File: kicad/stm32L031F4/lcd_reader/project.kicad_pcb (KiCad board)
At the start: 2 copper layers, 33 x 25.4 mm, 32 parts, among them J1 WAKE, J10 TEST_1P, J11 TEST_1P, J12 TEST_1P, J2 SWD, J3 TEST_1P, J4 TEST_1P, J5 TEST_1P, J6 LCD, J7 TEST_1P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

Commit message: All connected
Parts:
- moved R2 15.2 mm to (191.8, 137.1)
- moved R1 2.02 mm to (190.9, 121.8)
- renumbered J1 to WAKE
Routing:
- net +BATT: track 20.2 -> 98.6 mm, vias 0 -> 1
- net GND: track 65.7 -> 127.4 mm, vias 0 -> 8
- net Net-(Q1-Pad4): track 19.7 -> 1.93 mm, vias 2 -> 0
- net RADIO_PWR: track 3.43 -> 14.6 mm, vias 0 -> 2
- net Net-(J6-Pad7): track 10.8 -> 13.5 mm
- net Net-(J6-Pad5): track 10.5 -> 8.14 mm, vias 0 -> 1
- net Net-(J6-Pad6): track 12.4 -> 10.1 mm
- net Net-(J6-Pad4): track 12.8 -> 10.7 mm, vias 0 -> 1
- net Net-(J6-Pad1): track 11.0 -> 9.19 mm, vias 0 -> 1
- net IN8: track 29.3 -> 30.6 mm
- net TX: track 13.6 -> 14.7 mm
- net Net-(J6-Pad3): track 14.1 -> 15.0 mm
- net SWDIO: track 10.8 -> 11.7 mm
- net Net-(J6-Pad2): track 12.6 -> 13.4 mm
- net Net-(R1-Pad1): track 4.16 -> 3.42 mm
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- added copper zone on B.Cu, net GND
- added copper zone on F.Cu, net GND
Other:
- net class Default: clearance 0.2032 -> 0.2
- rule trace_clearance: 0.2032 -> 0.2

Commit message: Labels
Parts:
- added J13: GND_EXT, Pin_Headers:Pin_Header_Straight_1x01_Pitch2.54mm, F.Cu at (199.4, 141.0)
- renumbered WAKE to J1
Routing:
- net GND: track 127.4 -> 130.4 mm
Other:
- board text added: "+"
- board text added: "-"
- board text added: "CLK"
- board text added: "COM1"
- board text added: "DIO"
- board text added: "FET"
- board text added: "GND"
- board text added: "RDY"
- board text added: "RST"
- board text added: "SWD"
- board text added: "TX"
- board text added: "VCC"
- board text added: "WAKE"

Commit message: Logos
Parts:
- added REF**: TheApiLogo, theapi:TheApiLogoSmall, B.Cu at (186.8, 121.4)
- added REF**: TheApiLogoTiny, theapi:TheApiLogoTiny, F.Cu at (199.0, 117.2)
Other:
- board text added: "github.com/theapi/bathroom_scales November 2017 v1.0"
- board text added: "github.com/theapi/bathroom_scales v1.0"

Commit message: Silkscreen tidying
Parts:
- J13: footprint Pin_Headers:Pin_Header_Straight_1x01_Pitch2.54mm -> theapi:Pin_Header_Straight_1x01_Pitch2.54mm
- J8: footprint Pin_Headers:Pin_Header_Straight_1x03_Pitch2.54mm -> theapi:Pin_Header_Straight_1x03_Pitch2.54mm
- moved J6 20.3 mm to (168.9, 141.0), turned to 180 degrees
- moved C3 0.47 mm to (188.6, 136.2)
- moved REF** 0.28 mm to (198.8, 117.4)
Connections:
- J6 pad 1: Net-(J6-Pad1) -> COM1
- J6 pad 9: COM1 -> Net-(J6-Pad9)
- R10 pad 2: Net-(J6-Pad1) -> Net-(J6-Pad9)
- R3 pad 2: Net-(J6-Pad8) -> Net-(J6-Pad2)
- R4 pad 2: Net-(J6-Pad7) -> Net-(J6-Pad3)
- R5 pad 2: Net-(J6-Pad6) -> Net-(J6-Pad4)
- R7 pad 2: Net-(J6-Pad4) -> Net-(J6-Pad6)
- R8 pad 2: Net-(J6-Pad3) -> Net-(J6-Pad7)
- R9 pad 2: Net-(J6-Pad2) -> Net-(J6-Pad8)
- U1 pad 11: Net-(J6-Pad6) -> Net-(J6-Pad4)
- U1 pad 5: Net-(J6-Pad8) -> Net-(J6-Pad2)
- U1 pad 9: Net-(J6-Pad7) -> Net-(J6-Pad3)
- U3 pad 11: Net-(J6-Pad2) -> Net-(J6-Pad8)
- U3 pad 13: Net-(J6-Pad1) -> Net-(J6-Pad9)
- U3 pad 5: Net-(J6-Pad4) -> Net-(J6-Pad6)
- U3 pad 9: Net-(J6-Pad3) -> Net-(J6-Pad7)
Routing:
- net Net-(J6-Pad9): track 0.00 -> 9.19 mm, vias 0 -> 1
- net Net-(J6-Pad1): track 9.19 -> 0.00 mm, vias 1 -> 0
- net Net-(J6-Pad7): track 13.5 -> 15.0 mm
- net Net-(J6-Pad3): track 15.0 -> 13.5 mm
- net RADIO_PWR: track 14.6 -> 15.6 mm
- net Net-(J6-Pad8): track 12.7 -> 13.4 mm, vias 0 -> 1
- net Net-(J6-Pad2): track 13.4 -> 12.7 mm, vias 1 -> 0
- net Net-(J6-Pad6): track 10.1 -> 10.7 mm
- net Net-(J6-Pad4): track 10.7 -> 10.1 mm
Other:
- board text added: "LCD"
- board text added: "o"

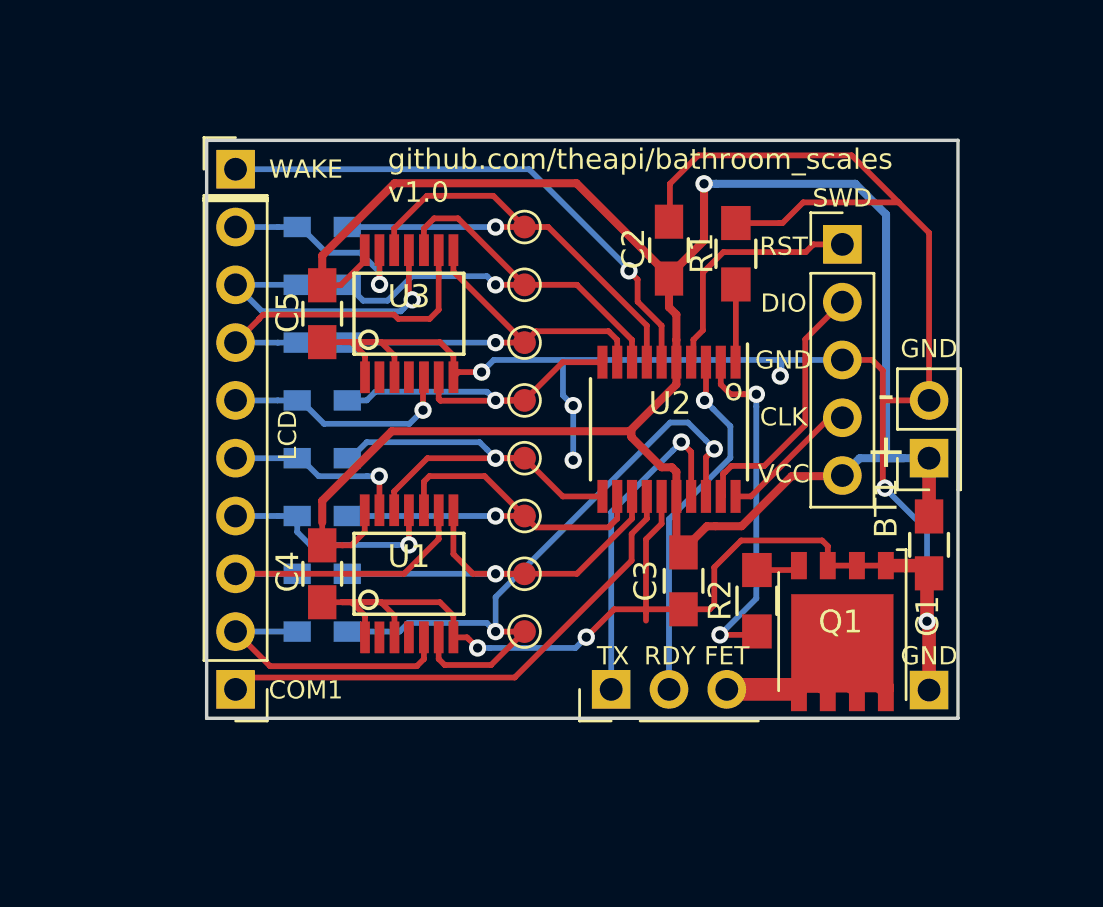
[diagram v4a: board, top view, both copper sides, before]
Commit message: Start of zebra strip compatability
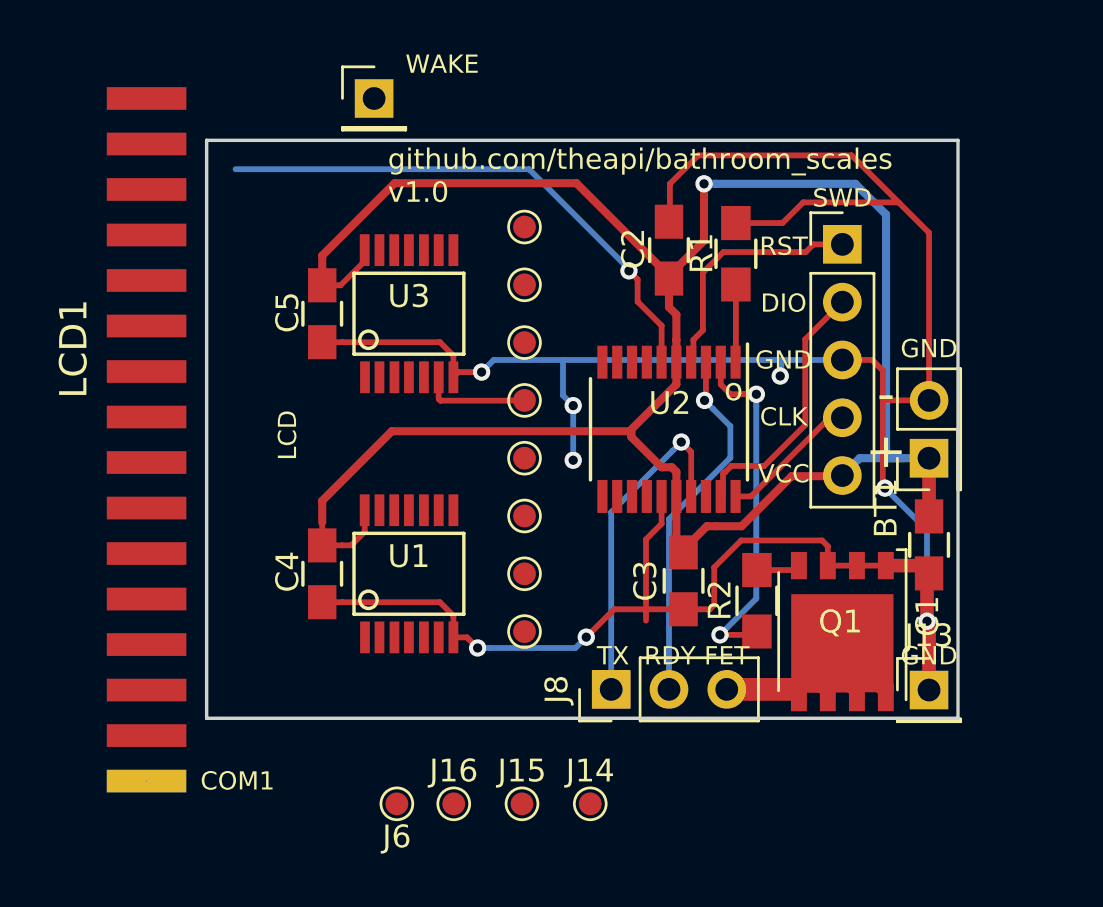
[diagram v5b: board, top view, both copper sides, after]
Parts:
- removed R10, R3, R4, R5, R6, R7, R8, R9: 0R, Resistors_SMD:R_0603_HandSoldering
- removed REF**: TheApiLogo, theapi:TheApiLogoSmall
- removed REF**: TheApiLogoTiny, theapi:TheApiLogoTiny
- added J14: TEST_1P, Connectors_TestPoints:Test_Point_Pad_d1.0mm, F.Cu at (184.5, 146.0)
- added J15: TEST_1P, Connectors_TestPoints:Test_Point_Pad_d1.0mm, F.Cu at (181.5, 146.0)
- added J16: TEST_1P, Connectors_TestPoints:Test_Point_Pad_d1.0mm, F.Cu at (178.5, 146.0)
- added LCD1: CONN_01X16, theapi:ZEBRA-16, F.Cu at (165.0, 126.0)
- J13: footprint theapi:Pin_Header_Straight_1x01_Pitch2.54mm -> Pin_Headers:Pin_Header_Straight_1x01_Pitch2.54mm
- J6: value LCD -> TEST_1P; footprint Pin_Headers:Pin_Header_Straight_1x09_Pitch2.54mm -> Connectors_TestPoints:Test_Point_Pad_d1.0mm
- J8: footprint theapi:Pin_Header_Straight_1x03_Pitch2.54mm -> Pin_Headers:Pin_Header_Straight_1x03_Pitch2.54mm
- moved J6 8.69 mm to (176.0, 146.0)
- moved J1 6.84 mm to (175.0, 115.0)
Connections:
- J6 pad 1: COM1 -> Net-(J6-Pad1)
- U1 pad 1: GND -> Net-(LCD1-Pad1)
- U1 pad 10: IN6 -> IN8
- U1 pad 11: Net-(J6-Pad4) -> Net-(LCD1-Pad5)
- U1 pad 12: IN5 -> IN7
- U1 pad 13: Net-(J6-Pad5) -> Net-(LCD1-Pad6)
- U1 pad 3: GND -> Net-(LCD1-Pad2)
- U1 pad 5: Net-(J6-Pad2) -> Net-(LCD1-Pad3)
- U1 pad 6: IN8 -> Net-(J14-Pad1)
- U1 pad 8: IN7 -> Net-(J6-Pad1)
- U1 pad 9: Net-(J6-Pad3) -> Net-(LCD1-Pad4)
- U3 pad 1: GND -> Net-(LCD1-Pad7)
- U3 pad 11: Net-(J6-Pad8) -> Net-(LCD1-Pad11)
- U3 pad 13: Net-(J6-Pad9) -> Net-(LCD1-Pad12)
- U3 pad 2: Net-(U3-Pad2) -> IN6
- U3 pad 3: GND -> Net-(LCD1-Pad8)
- U3 pad 4: Net-(U3-Pad4) -> IN5
- U3 pad 5: Net-(J6-Pad6) -> Net-(LCD1-Pad9)
- U3 pad 9: Net-(J6-Pad7) -> Net-(LCD1-Pad10)
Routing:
- net IN8: track 30.6 -> 0.00 mm, vias 2 -> 0
- net IN1: track 24.4 -> 0.00 mm, vias 1 -> 0
- net COM1: track 22.8 -> 0.00 mm
- net IN2: track 22.2 -> 0.00 mm, vias 1 -> 0
- net IN7: track 19.9 -> 0.00 mm, vias 1 -> 0
- net IN6: track 19.7 -> 0.00 mm, vias 1 -> 0
- net IN5: track 19.7 -> 0.00 mm, vias 1 -> 0
- net IN3: track 18.6 -> 0.00 mm, vias 1 -> 0
- net Net-(J6-Pad7): track 15.0 -> 0.00 mm
- net Net-(J6-Pad3): track 13.5 -> 0.00 mm
- net Net-(J6-Pad8): track 13.4 -> 0.00 mm, vias 1 -> 0
- net Net-(J6-Pad2): track 12.7 -> 0.00 mm
- net IN4: track 17.0 -> 4.76 mm, vias 1 -> 0
- net GND: track 130.0 -> 118.7 mm
- net Net-(J6-Pad6): track 10.7 -> 0.00 mm, vias 1 -> 0
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
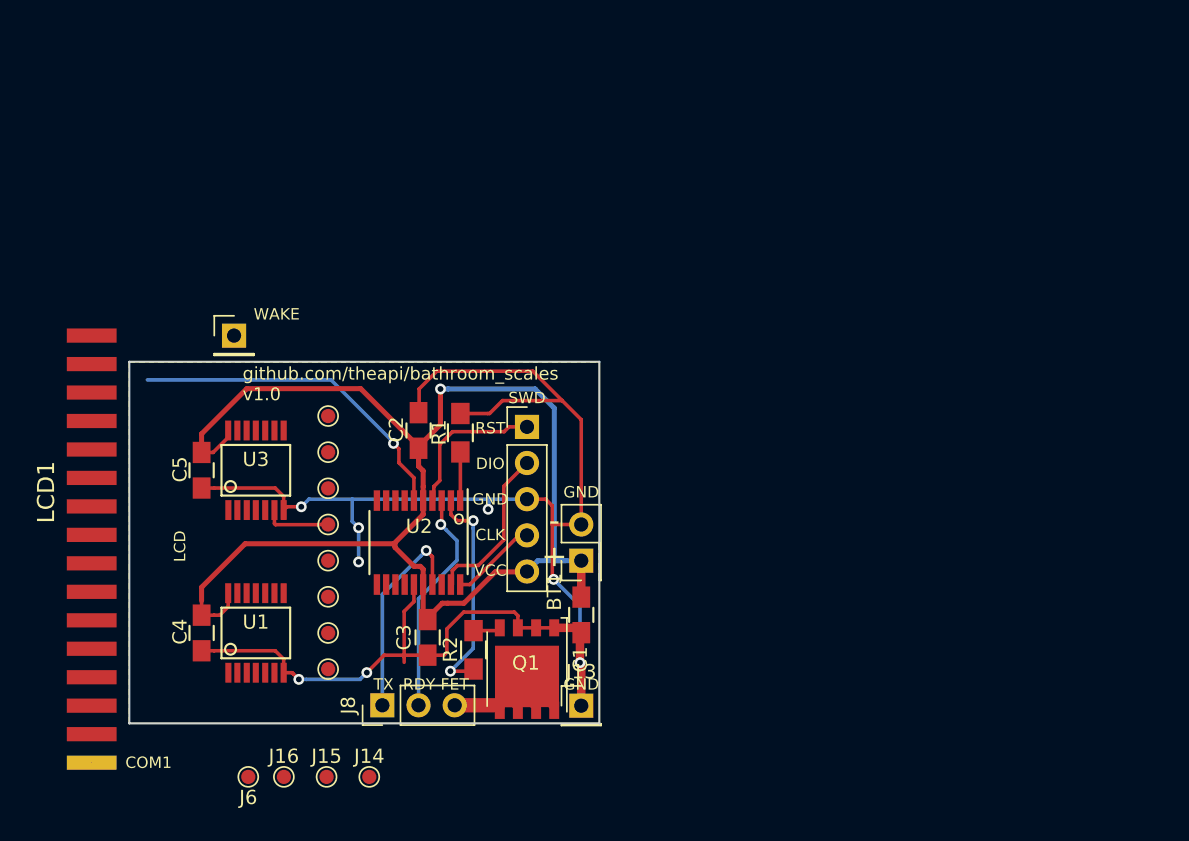
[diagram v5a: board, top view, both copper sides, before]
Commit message: Layout for sandwiched zebra connector
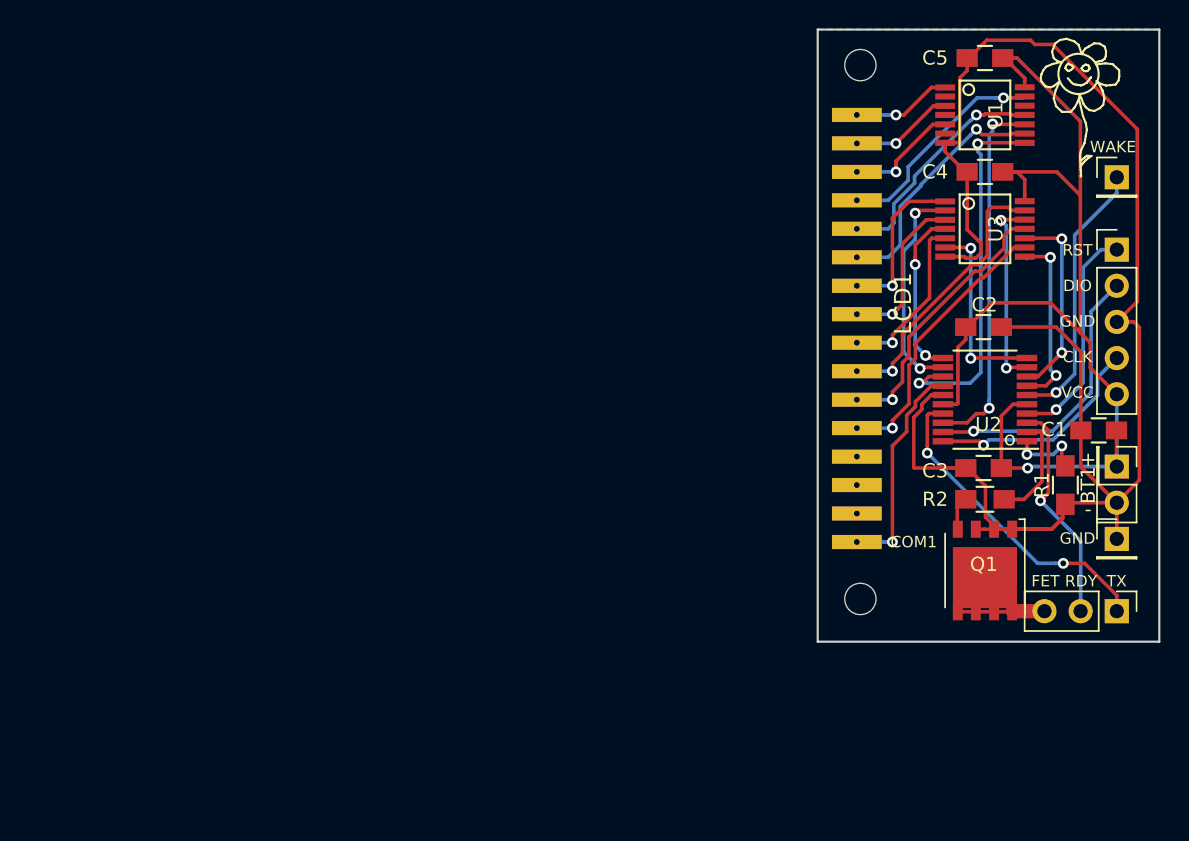
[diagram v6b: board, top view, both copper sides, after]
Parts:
- removed J10, J11, J12, J14, J15, J16, J3, J4, J5, J6, J7, J9: TEST_1P, Connectors_TestPoints:Test_Point_Pad_d1.0mm
- added REF**: MountingHole_2.2mm_M2, Mounting_Holes:MountingHole_2.2mm_M2, F.Cu at (219.0, 133.5)
- added REF**: TheApiLogo, theapi:TheApiLogoSmall, F.Cu at (235.0, 93.8)
- added REF**: TheApiLogoTiny, theapi:TheApiLogoTiny, F.Cu at (223.5, 130.8)
- added REF**: TheApiLogo, theapi:TheApiLogoSmall, B.Cu at (233.8, 129.5)
- added REF**: MountingHole_2.2mm_M2, Mounting_Holes:MountingHole_2.2mm_M2, F.Cu at (219.0, 96.0)
- moved C4 63.9 mm to (227.8, 103.5), turned to 0 degrees
- moved J1 63.0 mm to (237.0, 103.9)
- moved U1 62.8 mm to (227.8, 99.5), turned to 270 degrees
- moved C5 62.2 mm to (227.8, 95.5), turned to 0 degrees
- moved LCD1 55.9 mm to (218.8, 110.5)
- moved U3 54.0 mm to (227.8, 107.5), turned to 270 degrees
- moved J8 52.0 mm to (237.0, 134.4), turned to 270 degrees
- moved J2 43.3 mm to (237.0, 109.0)
- moved R1 42.7 mm to (233.4, 125.5), turned to 270 degrees
- moved U2 41.0 mm to (227.8, 119.5), turned to 180 degrees
- moved C3 40.8 mm to (227.7, 124.3), turned to 0 degrees
- moved C2 40.3 mm to (227.7, 114.4), turned to 0 degrees
- moved J13 39.4 mm to (237.0, 129.3)
- moved C1 38.6 mm to (235.7, 121.7), turned to 180 degrees
- moved BT1 38.2 mm to (237.0, 124.2), turned to 270 degrees
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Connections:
- U1 pad 12: IN7 -> Net-(U1-Pad12)
- U1 pad 13: Net-(LCD1-Pad6) -> Net-(LCD1-Pad4)
- U1 pad 8: Net-(J6-Pad1) -> IN7
- U1 pad 9: Net-(LCD1-Pad4) -> Net-(LCD1-Pad6)
- U3 pad 12: IN1 -> IN3
- U3 pad 13: Net-(LCD1-Pad12) -> Net-(LCD1-Pad10)
- U3 pad 8: IN3 -> IN1
- U3 pad 9: Net-(LCD1-Pad10) -> Net-(LCD1-Pad12)
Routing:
- net IN8: track 0.00 -> 26.1 mm, vias 0 -> 2
- net IN7: track 0.00 -> 26.0 mm, vias 0 -> 2
- net +BATT: track 98.4 -> 77.6 mm
- net Net-(LCD1-Pad12): track 0.00 -> 19.6 mm, vias 0 -> 1
- net Net-(LCD1-Pad10): track 0.00 -> 19.6 mm, vias 0 -> 1
- net Net-(LCD1-Pad11): track 0.00 -> 19.2 mm, vias 0 -> 1
- net /RADIO_GND: track 26.8 -> 9.30 mm
- net Net-(LCD1-Pad6): track 0.00 -> 17.4 mm, vias 0 -> 1
- net COM1: track 0.00 -> 16.7 mm, vias 0 -> 1
- net Net-(LCD1-Pad5): track 0.00 -> 16.3 mm, vias 0 -> 1
- net IN6: track 0.00 -> 15.7 mm, vias 0 -> 2
- net Net-(LCD1-Pad4): track 0.00 -> 15.4 mm, vias 0 -> 1
- net IN2: track 0.00 -> 13.8 mm, vias 0 -> 2
- net IN3: track 0.00 -> 13.7 mm, vias 0 -> 2
- net IN1: track 0.00 -> 12.8 mm, vias 0 -> 2
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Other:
- board size 33 x 25.4 mm -> 24 x 43 mm
- board text removed: "LCD"
- board text removed: "SWD"
- board text removed: "github.com/theapi/bathroom_scales v1.0"

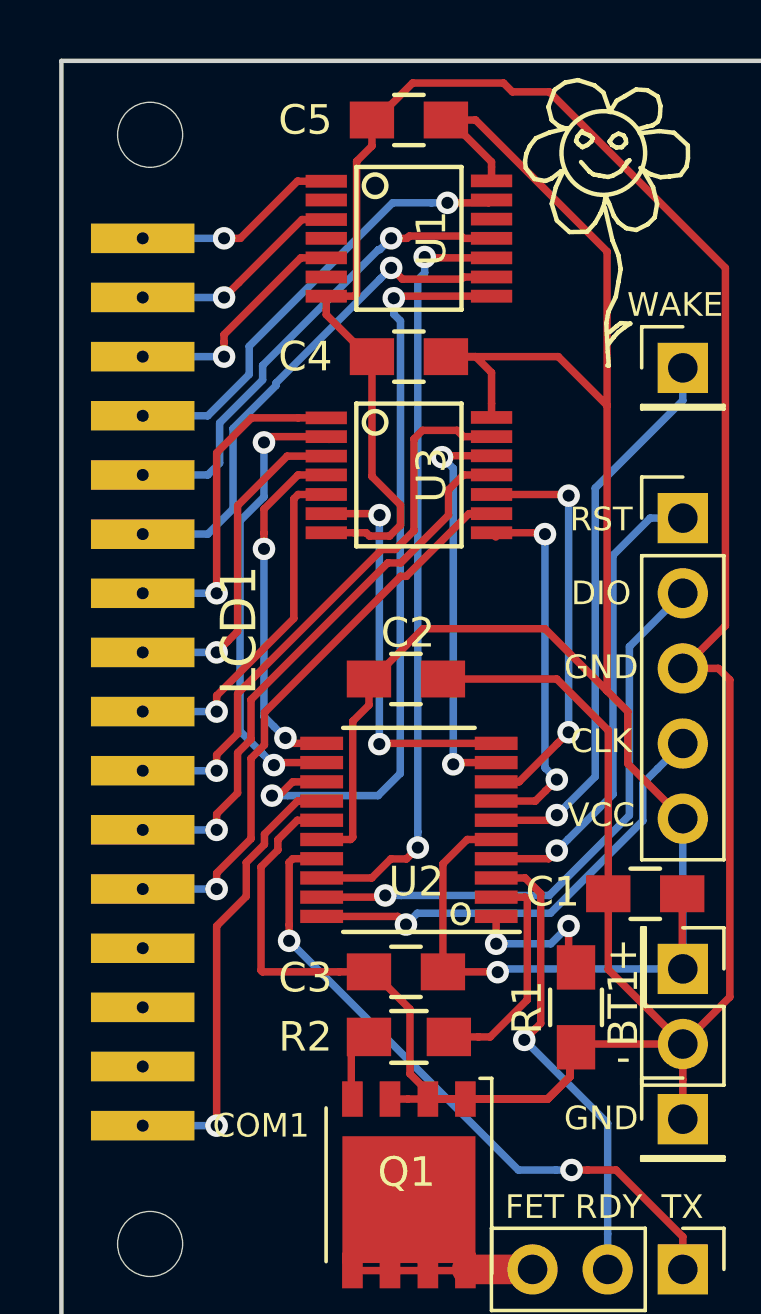
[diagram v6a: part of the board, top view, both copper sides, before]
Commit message: Main zebra connection on the top
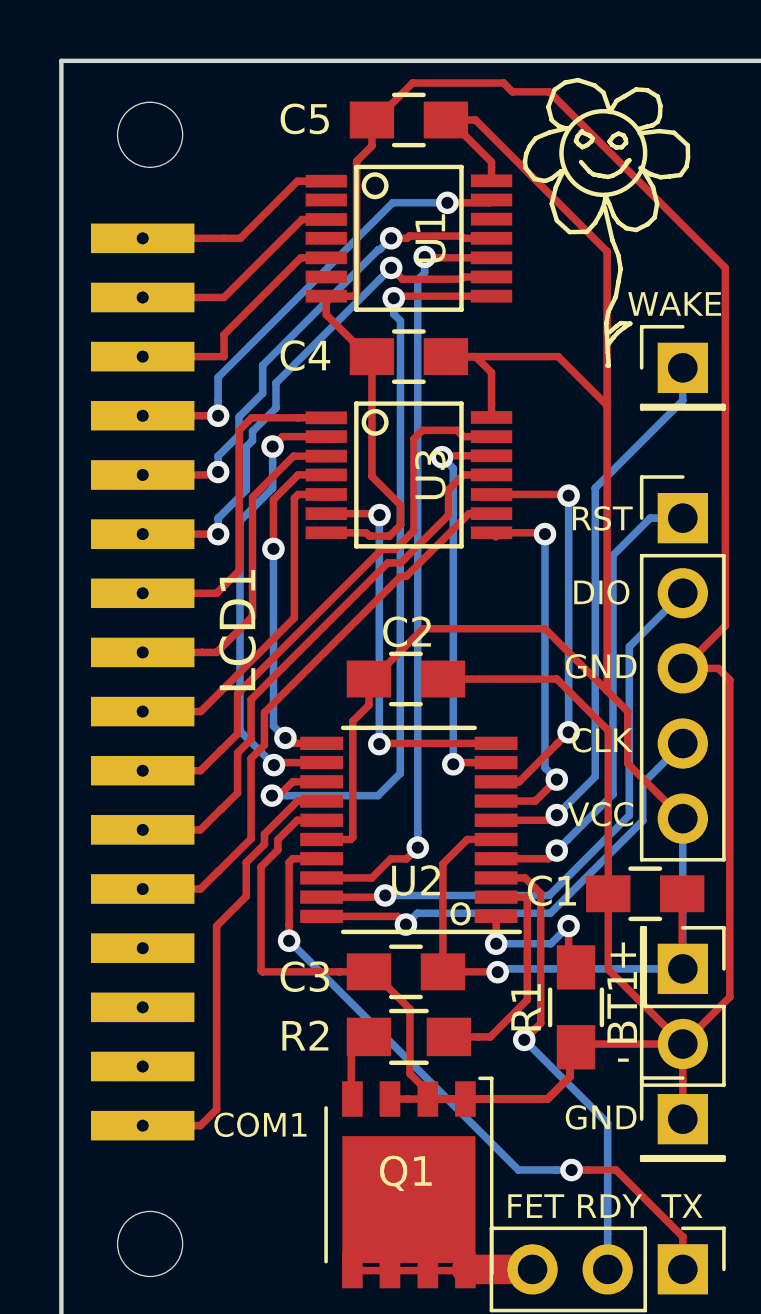
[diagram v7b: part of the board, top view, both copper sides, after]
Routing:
- net COM1: track 16.7 -> 15.1 mm, vias 1 -> 0
- net Net-(LCD1-Pad7): track 12.5 -> 11.4 mm, vias 1 -> 0
- net Net-(LCD1-Pad12): track 19.6 -> 19.3 mm, vias 1 -> 0
- net Net-(LCD1-Pad11): track 19.2 -> 18.8 mm, vias 1 -> 0
- net Net-(LCD1-Pad10): track 19.6 -> 19.3 mm, vias 1 -> 0
- net Net-(LCD1-Pad9): track 11.9 -> 11.6 mm, vias 1 -> 0
- net Net-(LCD1-Pad6): track 17.4 -> 17.6 mm, vias 1 -> 2
- net Net-(LCD1-Pad4): track 15.4 -> 15.6 mm, vias 1 -> 2
- net Net-(LCD1-Pad5): track 16.3 -> 16.4 mm, vias 1 -> 2
- net Net-(LCD1-Pad8): track 11.4 -> 11.3 mm, vias 1 -> 0
- net Net-(LCD1-Pad2): vias 1 -> 0
- net Net-(LCD1-Pad3): vias 1 -> 0
- net Net-(LCD1-Pad1): vias 1 -> 0
